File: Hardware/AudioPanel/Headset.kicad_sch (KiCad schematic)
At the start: 42 parts, among them J10 AudioJack3_Ground, J11 AudioJack3_Ground, J4 8P8C Jack

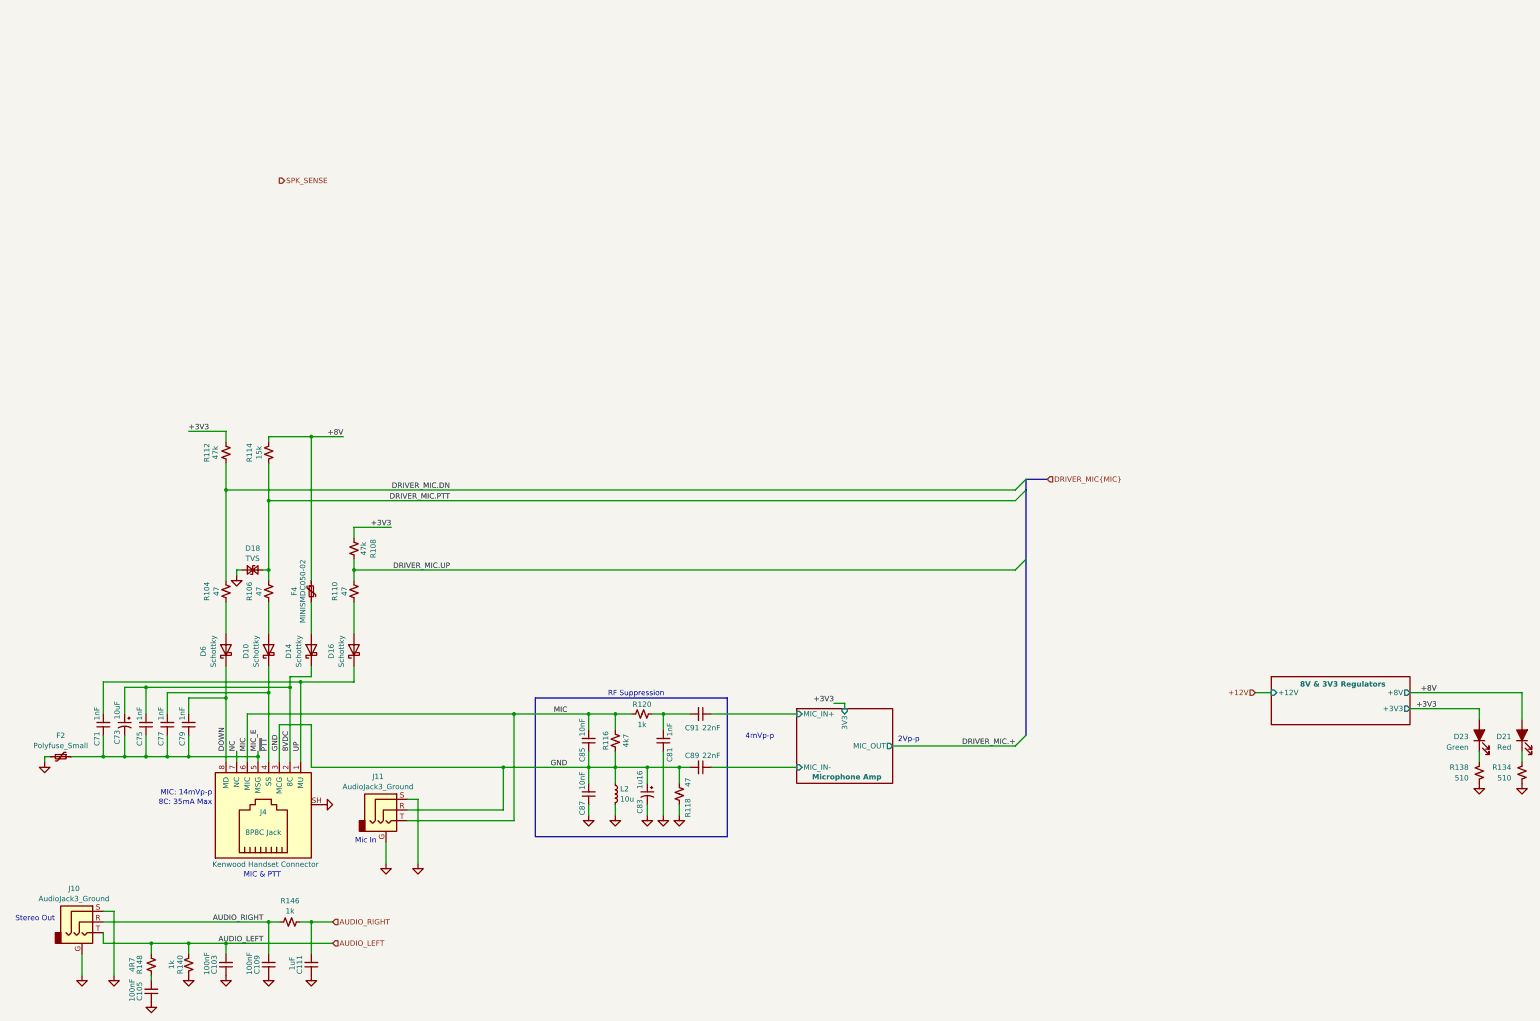
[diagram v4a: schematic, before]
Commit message: Realized that I need to rethink how I'm going to mix the radio audio with the stereo audio
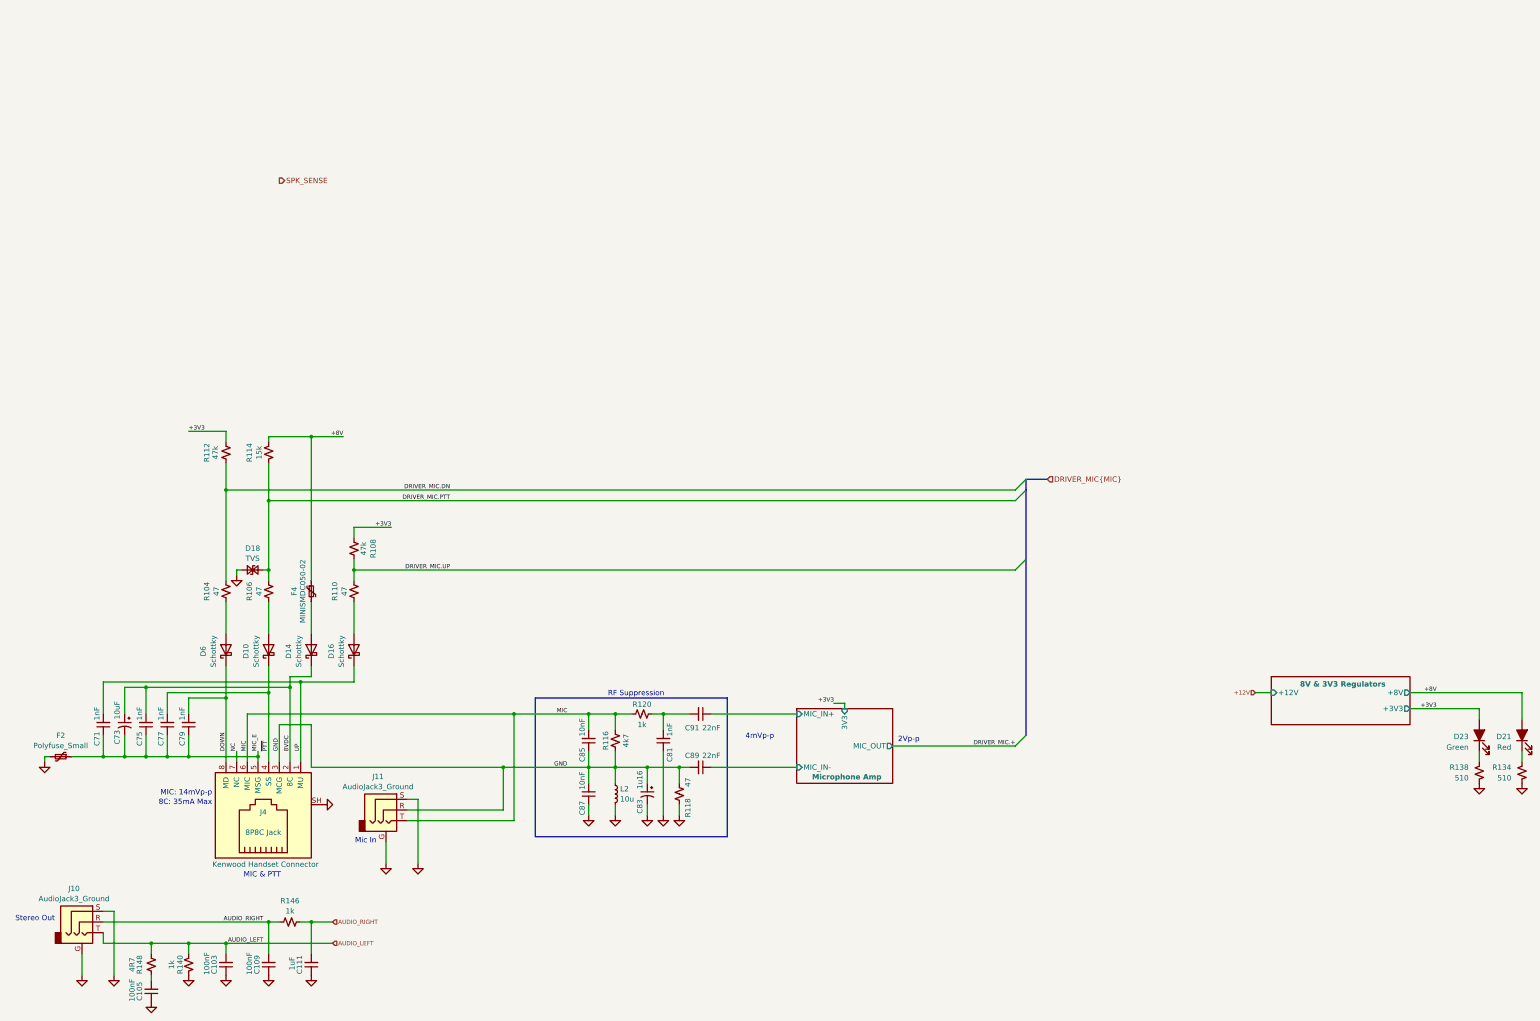
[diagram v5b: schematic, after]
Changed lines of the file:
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@@
 		(effects
 			(font
-				(size 1.27 1.27)
+				(size 1 1)
 			)
 			(justify right bottom)
@@
 		(effects
 			(font
-				(size 1.27 1.27)
+				(size 1 1)
 			)
 			(justify right bottom)
@@
 		(effects
 			(font
-				(size 1.27 1.27)
+				(size 1 1)
 			)
 			(justify left bottom)
@@
 		(effects
 			(font
-				(size 1.27 1.27)
+				(size 1 1)
 			)
 			(justify left bottom)
@@
 		(effects
 			(font
-				(size 1.27 1.27)
+				(size 1 1)
 			)
 			(justify right bottom)
@@
 		(effects
 			(font
-				(size 1.27 1.27)
+				(size 1 1)
 			)
 			(justify right bottom)
@@
 		(effects
 			(font
-				(size 1.27 1.27)
+				(size 1 1)
 			)
 			(justify right bottom)
@@
 		(effects
 			(font
-				(size 1.27 1.27)
+				(size 1 1)
 			)
 			(justify left bottom)
@@
 		(effects
 			(font
-				(size 1.27 1.27)
+				(size 1 1)
 			)
 			(justify right bottom)
@@
 		(effects
 			(font
-				(size 1.27 1.27)
+				(size 1 1)
 			)
 			(justify right bottom)
@@
 		(effects
 			(font
-				(size 1.27 1.27)
+				(size 1 1)
 			)
 			(justify left bottom)
@@
 		(effects
 			(font
-				(size 1.27 1.27)
+				(size 1 1)
 			)
 			(justify right bottom)
@@
 		(effects
 			(font
-				(size 1.27 1.27)
+				(size 1 1)
 			)
 			(justify right bottom)
@@
 		(effects
 			(font
-				(size 1.27 1.27)
+				(size 1 1)
 			)
 			(justify left bottom)
@@
 		(effects
 			(font
-				(size 1.27 1.27)
+				(size 1 1)
 			)
 			(justify right bottom)
@@
 		(effects
 			(font
-				(size 1.27 1.27)
+				(size 1 1)
 			)
 			(justify left bottom)
@@
 		(effects
 			(font
-				(size 1.27 1.27)
+				(size 1 1)
 			)
 			(justify left bottom)
@@
 		(effects
 			(font
-				(size 1.27 1.27)
+				(size 1 1)
 			)
 			(justify right bottom)
@@
 		(effects
 			(font
-				(size 1.27 1.27)
+				(size 1 1)
 			)
 			(justify right bottom)
@@
 		(effects
 			(font
-				(size 1.27 1.27)
+				(size 1 1)
 			)
 			(justify left bottom)
@@
 		(effects
 			(font
-				(size 1.27 1.27)
+				(size 1 1)
 			)
 			(justify left bottom)
@@
 		(effects
 			(font
-				(size 1.27 1.27)
+				(size 1 1)
 			)
 			(justify right bottom)
@@
 		(effects
 			(font
-				(size 1.27 1.27)
+				(size 1 1)
 			)
 			(justify left)
@@
 		(effects
 			(font
-				(size 1.27 1.27)
+				(size 1 1)
 			)
 			(justify right)
@@
 		(effects
 			(font
-				(size 1.27 1.27)
+				(size 1 1)
 			)
 			(justify left)

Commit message: Added speaker and headphone audio switching
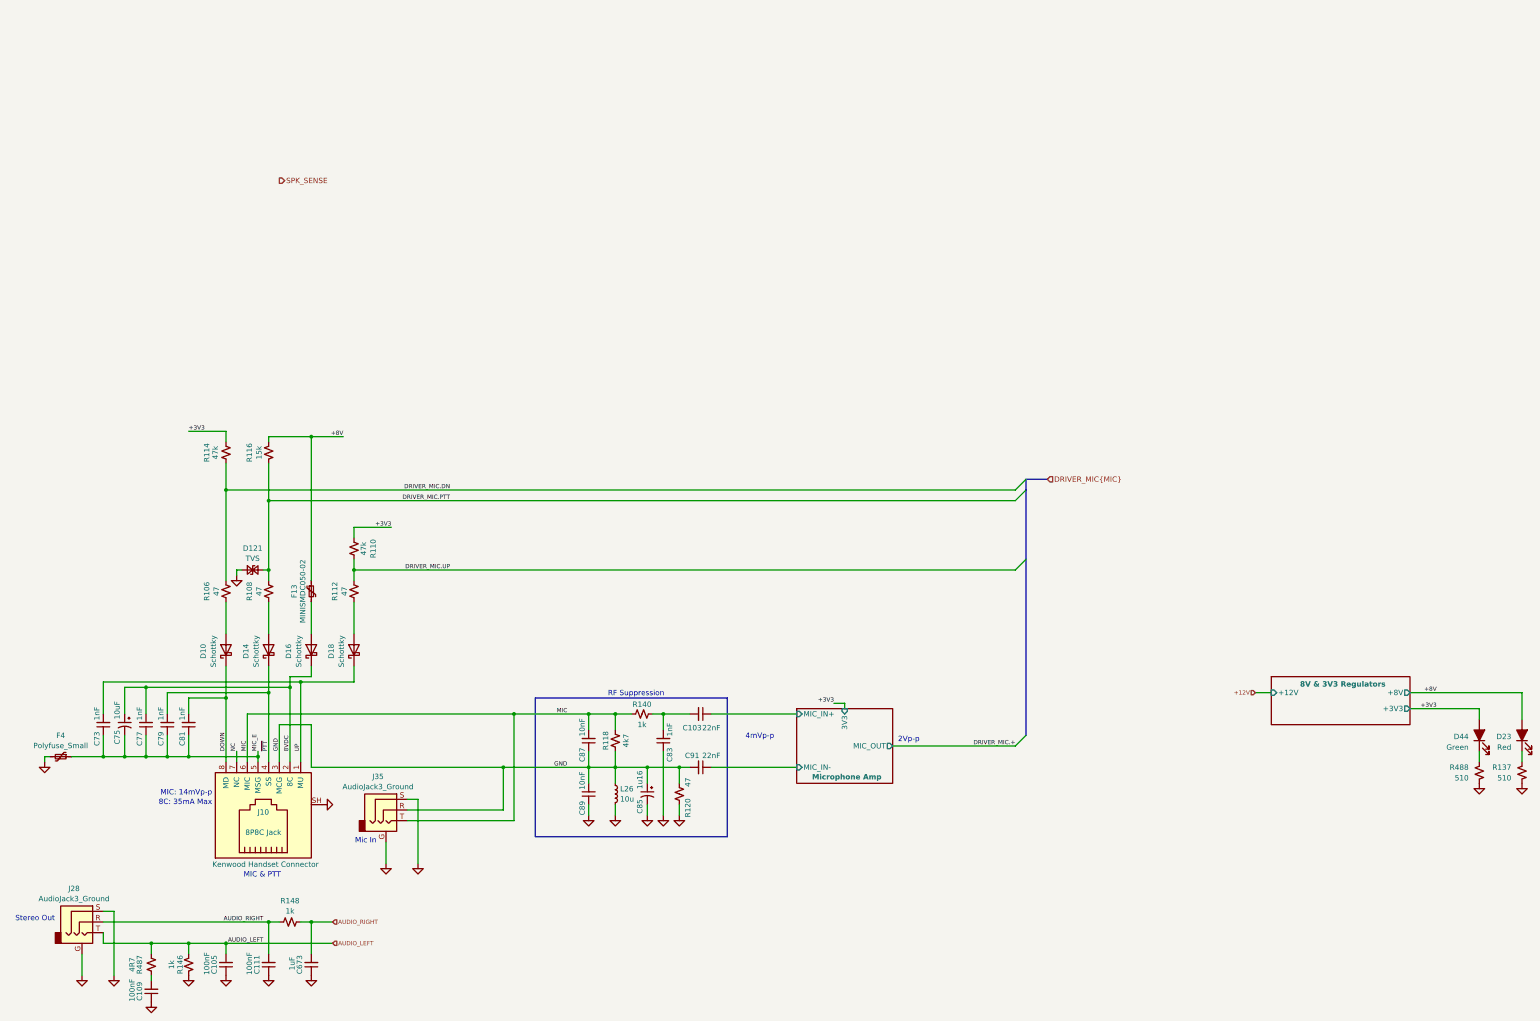
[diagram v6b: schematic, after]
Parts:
- renumbered C91 to C103, C103 to C105, C105 to C109, C109 to C111, C111 to C673, C71 to C73, C73 to C75, C75 to C77, C77 to C79, C79 to C81, C81 to C83, C83 to C85, C85 to C87, C87 to C89, C89 to C91, D6 to D10, D18 to D121, D10 to D14, D14 to D16, D16 to D18, D21 to D23, D23 to D44, F4 to F13, F2 to F4, J4 to J10, J10 to J28, J11 to J35, L2 to L26, R104 to R106, R106 to R108, R108 to R110, R110 to R112, R112 to R114, R114 to R116, R116 to R118, R118 to R120, R134 to R137, R120 to R140, R140 to R146, R146 to R148, R148 to R487, R138 to R488
